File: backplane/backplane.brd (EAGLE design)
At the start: 101.6 x 123.2 mm, 4 parts

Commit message: Updated backplane with all topside traces, correct planes.
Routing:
- net SPARE28: track 0.00 -> 100.1 mm
- net SCL_ESC: track 32.8 -> 98.4 mm
- net SPARE27: track 100.7 -> 99.0 mm
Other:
- board text removed: "BACKPLANE"

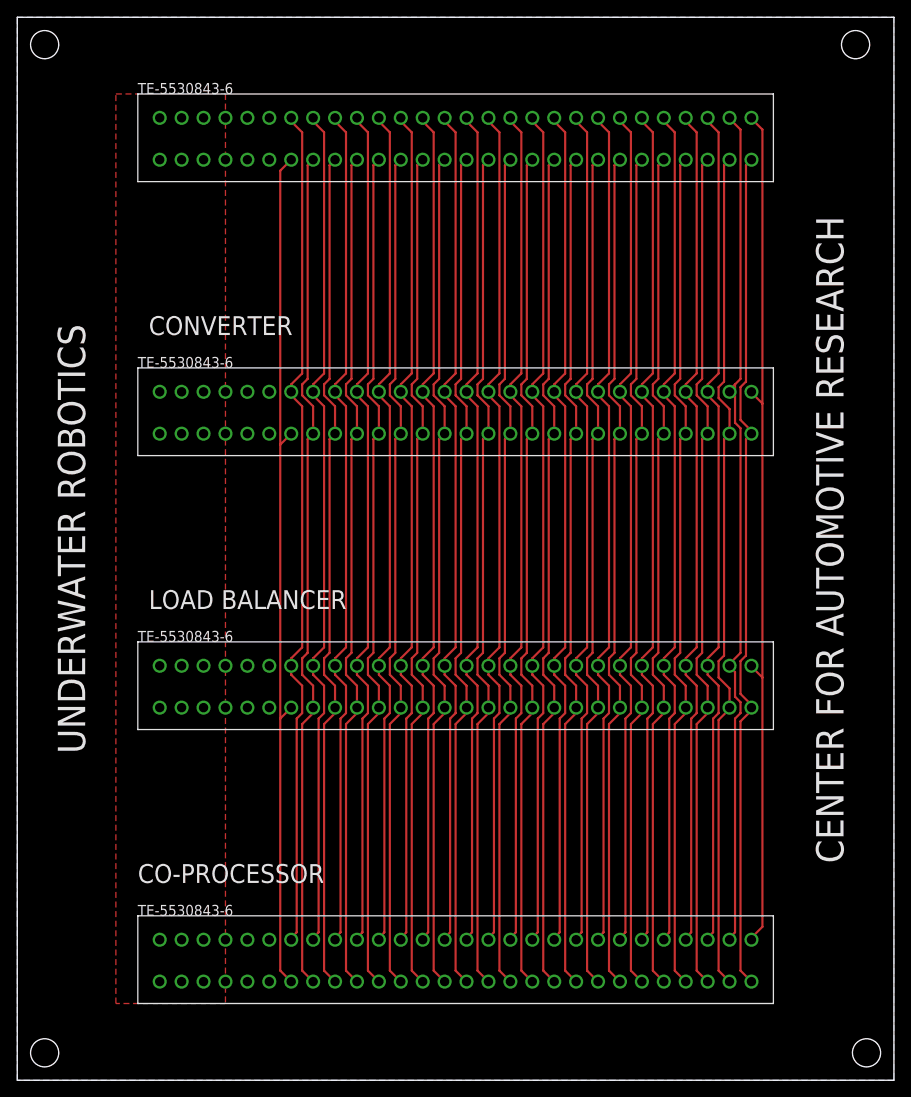
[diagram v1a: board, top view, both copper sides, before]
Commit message: Re-do with dimensions agreeing with mechanical team
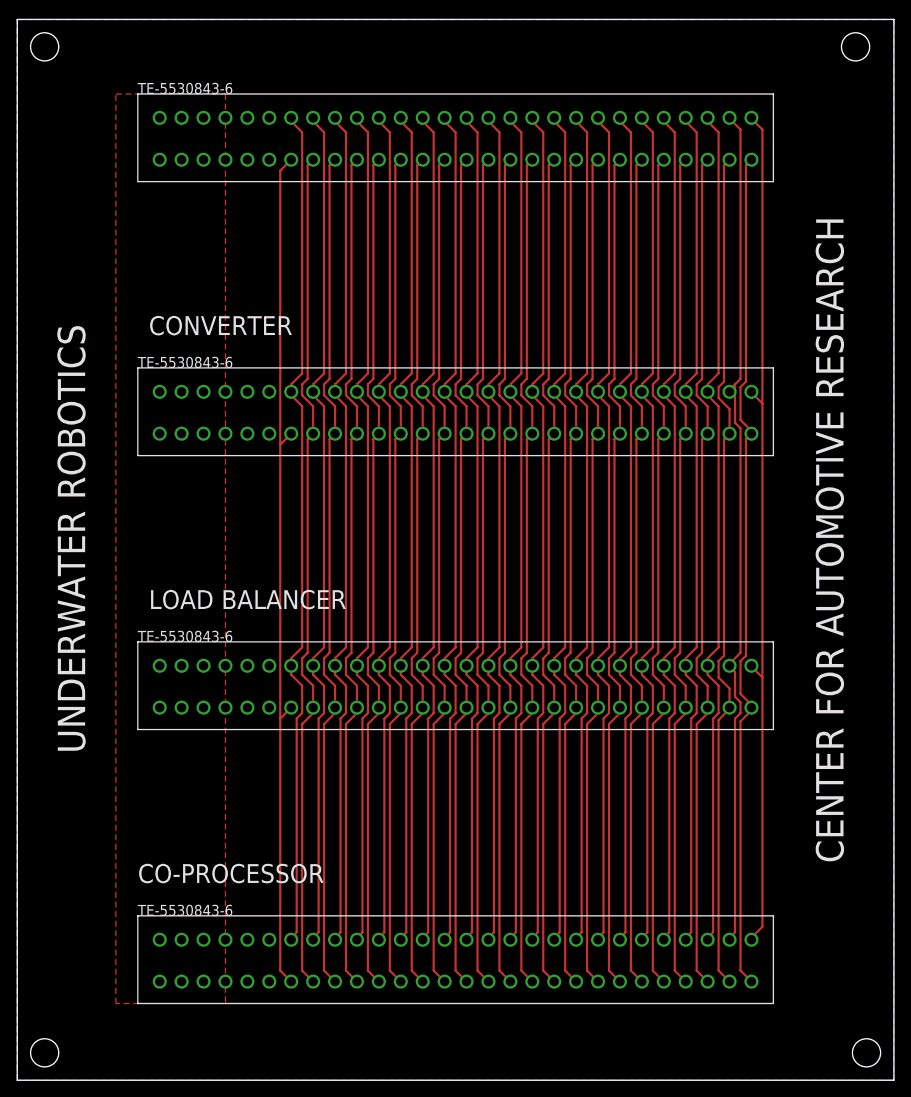
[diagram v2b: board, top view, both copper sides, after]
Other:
- board size 101.6 x 123.2 mm -> 101.6 x 122.9 mm
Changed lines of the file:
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@@
 <setting verticaltext="up"/>
 </settings>
-<grid distance="0.02" unitdist="inch" unit="inch" style="lines" multiple="1" display="yes" altdistance="0.025" altunitdist="inch" altunit="inch"/>
+<grid distance="0.01" unitdist="inch" unit="inch" style="lines" multiple="1" display="yes" altdistance="0.025" altunitdist="inch" altunit="inch"/>
 <layers>
 <layer number="1" name="Top" color="4" fill="1" visible="yes" active="yes"/>
@@
 <layer number="27" name="tValues" color="7" fill="1" visible="yes" active="yes"/>
 <layer number="28" name="bValues" color="7" fill="1" visible="yes" active="yes"/>
-<layer number="29" name="tStop" color="7" fill="3" visible="no" active="yes"/>
-<layer number="30" name="bStop" color="7" fill="6" visible="no" active="yes"/>
-<layer number="31" name="tCream" color="7" fill="4" visible="no" active="yes"/>
-<layer number="32" name="bCream" color="7" fill="5" visible="no" active="yes"/>
-<layer number="33" name="tFinish" color="6" fill="3" visible="no" active="yes"/>
-<layer number="34" name="bFinish" color="6" fill="6" visible="no" active="yes"/>
-<layer number="35" name="tGlue" color="7" fill="4" visible="no" active="yes"/>
-<layer number="36" name="bGlue" color="7" fill="5" visible="no" active="yes"/>
-<layer number="37" name="tTest" color="7" fill="1" visible="no" active="yes"/>
-<layer number="38" name="bTest" color="7" fill="1" visible="no" active="yes"/>
+<layer number="29" name="tStop" color="7" fill="3" visible="yes" active="yes"/>
+<layer number="30" name="bStop" color="7" fill="6" visible="yes" active="yes"/>
+<layer number="31" name="tCream" color="7" fill="4" visible="yes" active="yes"/>
+<layer number="32" name="bCream" color="7" fill="5" visible="yes" active="yes"/>
+<layer number="33" name="tFinish" color="6" fill="3" visible="yes" active="yes"/>
+<layer number="34" name="bFinish" color="6" fill="6" visible="yes" active="yes"/>
+<layer number="35" name="tGlue" color="7" fill="4" visible="yes" active="yes"/>
+<layer number="36" name="bGlue" color="7" fill="5" visible="yes" active="yes"/>
+<layer number="37" name="tTest" color="7" fill="1" visible="yes" active="yes"/>
+<layer number="38" name="bTest" color="7" fill="1" visible="yes" active="yes"/>
 <layer number="39" name="tKeepout" color="4" fill="11" visible="yes" active="yes"/>
 <layer number="40" name="bKeepout" color="1" fill="11" visible="yes" active="yes"/>
@@
 <layer number="42" name="bRestrict" color="1" fill="10" visible="yes" active="yes"/>
 <layer number="43" name="vRestrict" color="2" fill="10" visible="yes" active="yes"/>
-<layer number="44" name="Drills" color="7" fill="1" visible="no" active="yes"/>
+<layer number="44" name="Drills" color="7" fill="1" visible="yes" active="yes"/>
 <layer number="45" name="Holes" color="7" fill="1" visible="yes" active="yes"/>
-<layer number="46" name="Milling" color="3" fill="1" visible="no" active="yes"/>
-<layer number="47" name="Measures" color="7" fill="1" visible="no" active="yes"/>
+<layer number="46" name="Milling" color="3" fill="1" visible="yes" active="yes"/>
+<layer number="47" name="Measures" color="7" fill="1" visible="yes" active="yes"/>
 <layer number="48" name="Document" color="7" fill="1" visible="yes" active="yes"/>
 <layer number="49" name="Reference" color="7" fill="1" visible="yes" active="yes"/>
@@
 <plain>
 <wire x1="0" y1="0" x2="101.6" y2="0" width="0" layer="20"/>
-<wire x1="101.6" y1="0" x2="101.6" y2="123.19" width="0" layer="20"/>
-<wire x1="101.6" y1="123.19" x2="0" y2="123.19" width="0" layer="20"/>
-<wire x1="0" y1="123.19" x2="0" y2="0" width="0" layer="20"/>
+<wire x1="101.6" y1="0" x2="101.6" y2="122.936" width="0" layer="20"/>
+<wire x1="101.6" y1="122.936" x2="0" y2="122.936" width="0" layer="20"/>
+<wire x1="0" y1="122.936" x2="0" y2="0" width="0" layer="20"/>
 <text x="95.758" y="25.146" size="3.175" layer="21" rot="R90">CENTER FOR AUTOMOTIVE RESEARCH</text>
 <text x="13.97" y="22.86" size="2.1844" layer="21">CO-PROCESSOR </text>
@@
 <text x="15.24" y="86.36" size="2.1844" layer="21">CONVERTER</text>
 <hole x="3.175" y="3.175" drill="3.2639"/>
-<hole x="3.175" y="120.015" drill="3.2639"/>
-<hole x="97.155" y="120.015" drill="3.2639"/>
+<hole x="3.175" y="119.761" drill="3.2639"/>
+<hole x="97.155" y="119.761" drill="3.2639"/>
 <hole x="98.425" y="3.175" drill="3.2639"/>
 <text x="7.874" y="37.846" size="3.175" layer="21" rot="R90">UNDERWATER ROBOTICS</text>
@@
 <contactref element="CONVERTER" pad="SPARE6"/>
 <polygon width="0.4064" layer="16">
-<vertex x="0" y="123.19"/>
-<vertex x="101.6" y="123.19"/>
+<vertex x="0" y="122.936"/>
+<vertex x="101.6" y="122.936"/>
 <vertex x="101.6" y="0"/>
 <vertex x="0" y="0"/>
